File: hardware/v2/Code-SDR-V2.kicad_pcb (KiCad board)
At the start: 4 copper layers, 160 x 100 mm, 344 parts, among them J1 5V_INPUT_ONLY, J10 USB_B_Micro, J11 Cortex_SWD_10pin, J30 JK0654219NL, J50 RF_LOW_0.1_2.5GHz, J60 RF_HIGH_2.3_4.2GHz, J61 RF_HIGH_4.2_6.8GHz, J62 RF_HIGH_6.8_9.2GHz, J63 RF_HIGH_8.0_10GHz, SW1 BOOTSEL, SW2 RESET, T50 2450BL15B0200001E, T60 TC1-1-13M+, T70 2450BL15B0100001E, U1 TLV62569DBVR, U10 RP2040, U11 W25Q16JVSSIQ, U12 USBLC6-2SC6, U2 TLV62569DBVR, U20 LIF-MD6000-6JMG80I, U21 AD9215BCPZ-105, U3 TLV75525PDBVR, U30 KSZ9031RNXCA, U4 TLV76733DRVR, U40 LMX2592RHAT, U41 ADF4360-1BCPZ, U42 CDCLVC1104PWR, U50 GRF4001, U51 ADL5801ACPZ-R7, U60 GRF4001, U61 GRF2101, U62 GRF2101, U63 LTC5548IUDB, U64 QPC6144TR13, U66 GRF2101, U67 GRF2101, U70 BGS12WN6E6327, U71 GRF2013, U72 PE4312C-Z, U73 LT5560EDD, U74 AD8351ARMZ, U75 GRF2013, Y10 ABM8-272-T3_12MHz, Y30 ECS-250-20-33-TR_25MHz, Y40 SiT8209AC-23-33E-100.000000X

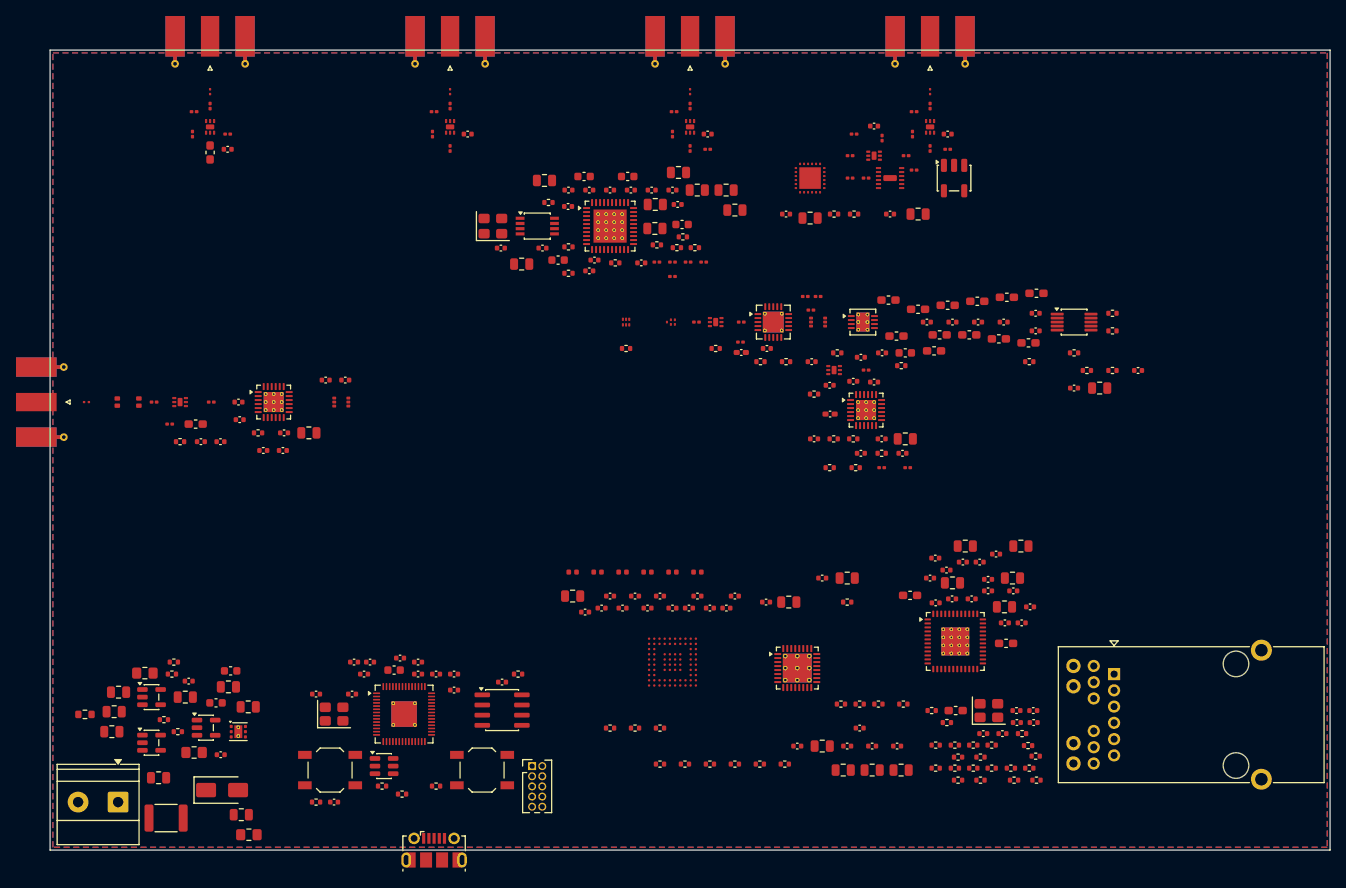
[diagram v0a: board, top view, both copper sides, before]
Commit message: hardware: finalize four-layer RF50 routing handoff
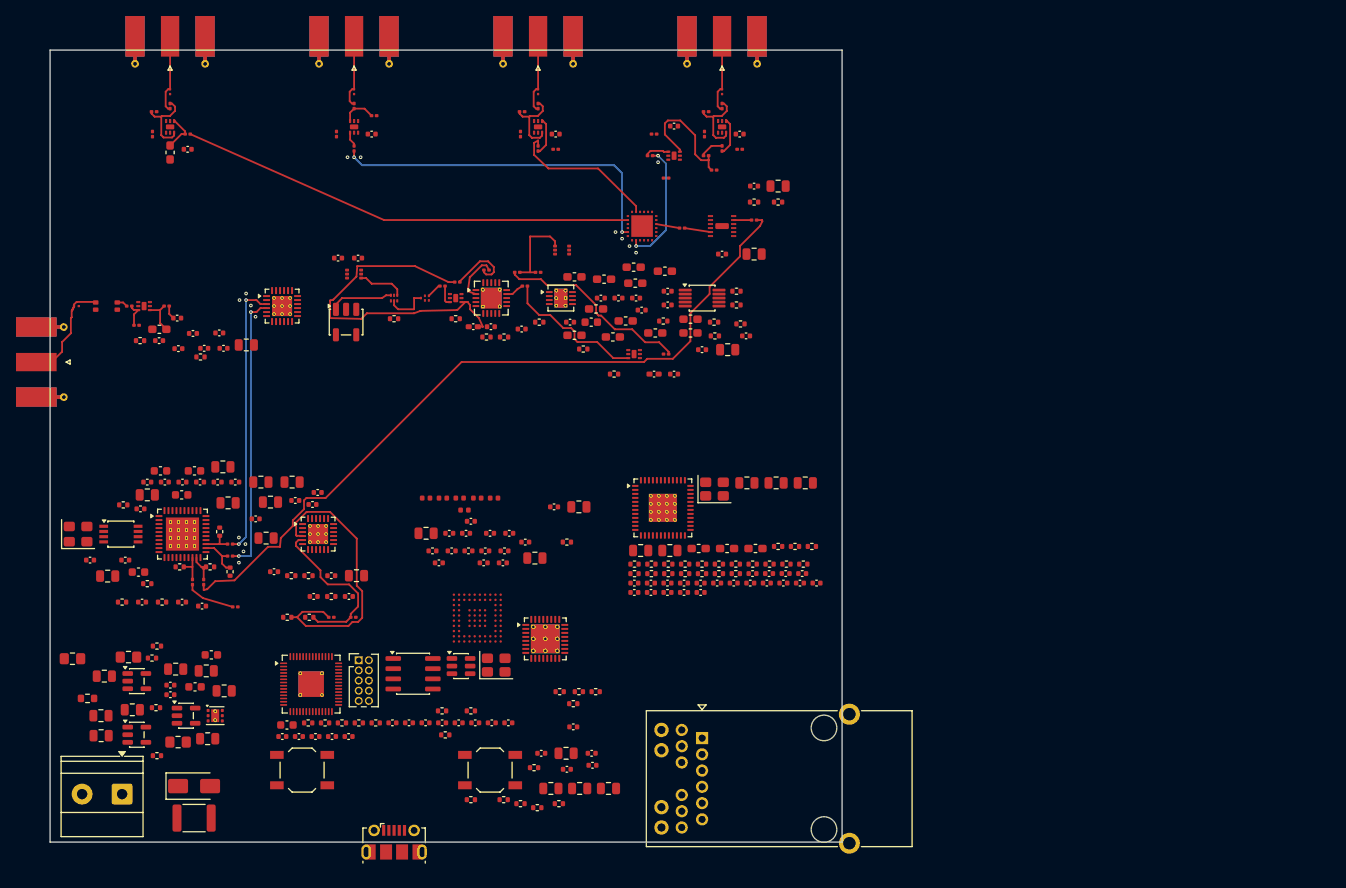
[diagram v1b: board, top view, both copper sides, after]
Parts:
- moved T60 78.1 mm to (37.0, 34.0)
- moved C71 75.4 mm to (11.5, 69.0)
- moved R56 74.8 mm to (9.00, 69.0)
- moved R53 73.9 mm to (16.2, 64.6)
- moved C202 72.1 mm to (17.8, 66.5), turned to -90 degrees
- moved C207 71.8 mm to (37.9, 70.9)
- moved C205 71.5 mm to (37.4, 68.3)
- moved C206 71.3 mm to (35.1, 70.9)
- moved R93 71.1 mm to (35.1, 68.3)
- moved C72 70.9 mm to (35.1, 65.7)
- moved R55 70.8 mm to (22.5, 65.2), turned to 90 degrees
- moved R95 70.8 mm to (32.4, 70.9)
- moved C75 70.7 mm to (33.0, 68.3)
- moved C73 70.7 mm to (38.3, 65.7)
- moved R94 70.3 mm to (29.6, 70.9)
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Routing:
- net LO_HIGH_P: track 0.00 -> 95.4 mm
- net RF_HA_LNA_OUT: track 0.00 -> 57.0 mm
- net GRF2013_RFOUT_VDD: track 0.00 -> 43.8 mm
- net RF_HB_LNA_OUT: track 0.00 -> 43.2 mm, vias 0 -> 2
- net ADF_LO2_P_RAW: track 0.00 -> 36.4 mm
- net LO_LOW_N: track 0.00 -> 34.9 mm, vias 0 -> 2
- net LO_LOW_P: track 0.00 -> 34.4 mm, vias 0 -> 2
- net IF_DSA_GAINED: track 0.00 -> 24.4 mm
- net ADF_LO2_N_RAW: track 0.00 -> 20.6 mm
- net RF_HC_LNA_OUT: track 0.00 -> 18.8 mm
- net IF_DSA_OUT: track 0.00 -> 18.2 mm
- net RF_HD_LNA_OUT: track 0.00 -> 15.7 mm, vias 0 -> 2
- net RF_HD_LNA2_IN: track 0.00 -> 15.3 mm
- net RF_LOW_IN: track 0.00 -> 11.1 mm
- net LT_INPUT_SE: track 0.00 -> 10.4 mm
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- added copper zone on In2.Cu, net GND
- removed copper zone on B.Cu, net GND
- removed copper zone on F.Cu, net GND
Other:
- board size 160 x 100 mm -> 99 x 99 mm
- board text added: "4-LAYER PLACEMENT ONLY / NO ESC"
- board text removed: "RECEIVER + CONTROL BOARD / NO ESC"

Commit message: Route and length-match Ethernet MDI pairs
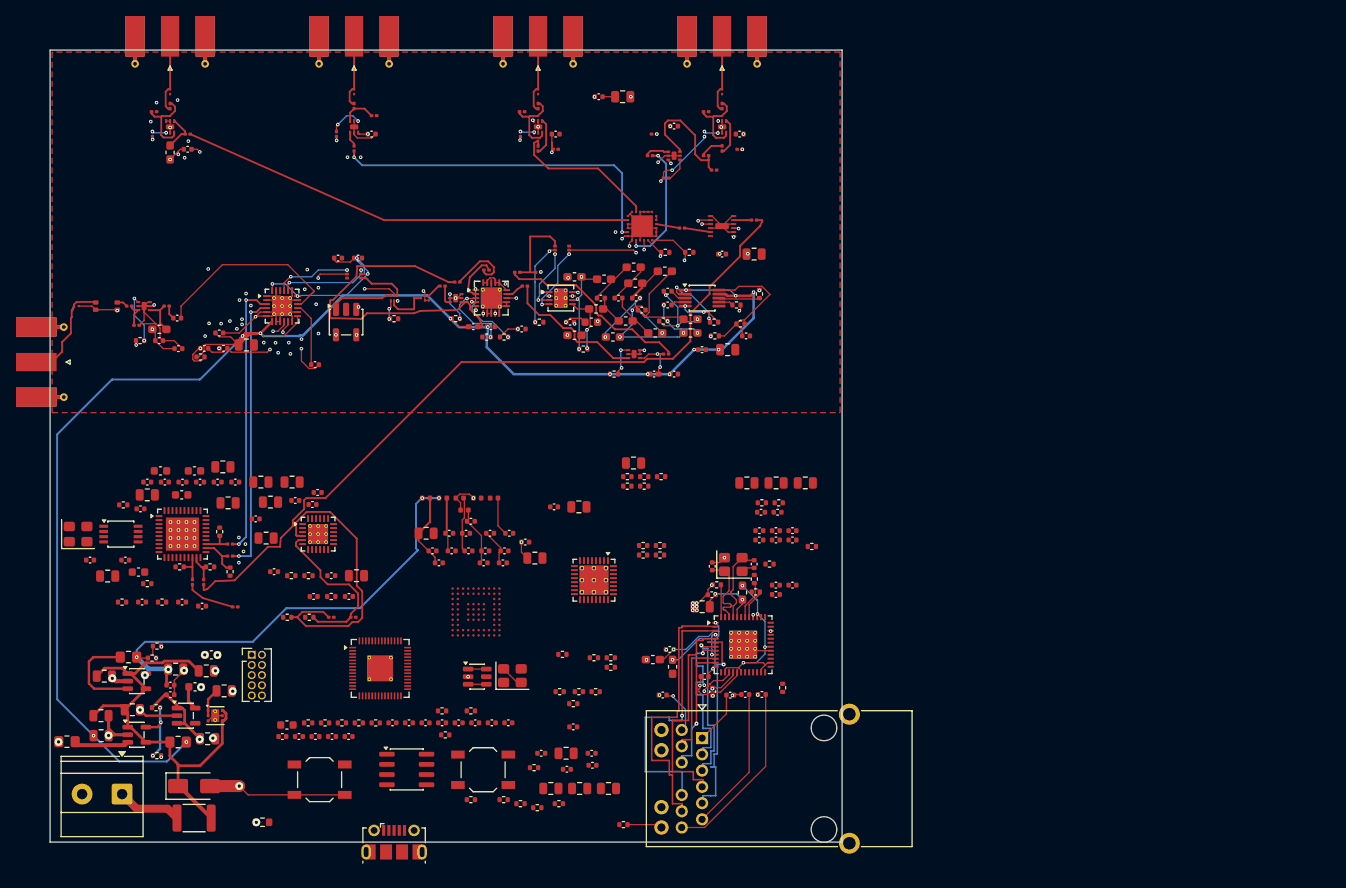
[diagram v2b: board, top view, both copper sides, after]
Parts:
- moved R42 33.6 mm to (71.7, 96.8)
- moved R5 26.8 mm to (26.6, 96.5)
- moved C260 22.4 mm to (68.6, 5.83)
- moved C261 22.4 mm to (71.6, 5.83), turned to 180 degrees
- moved C153 22.1 mm to (76.6, 80.6), turned to 180 degrees
- moved U30 19.8 mm to (86.6, 74.3)
- moved R43 19.5 mm to (70.1, 77.2)
- moved R132 19.5 mm to (68.0, 76.0)
- moved R133 19.5 mm to (70.1, 76.0)
- moved C50 18.8 mm to (82.8, 80.2), turned to -90 degrees
- moved FB32 18.1 mm to (77.8, 77.1), turned to 90 degrees
- moved C301 16.9 mm to (88.7, 60.1)
- moved C302 16.9 mm to (90.7, 60.1)
- moved C303 16.9 mm to (92.8, 60.1)
- moved C51 16.9 mm to (88.7, 61.2)
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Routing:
- net +5V_RF: track 0.00 -> 225.9 mm, vias 0 -> 18
- net GND: track 0.00 -> 202.4 mm, vias 15 -> 84
- net +1V2_CORE: track 0.00 -> 81.5 mm, vias 0 -> 8
- net +3V3_DIG: track 0.00 -> 80.8 mm, vias 0 -> 16
- net VIN_FUSED: track 0.00 -> 57.5 mm
- net IF_HIGH_P: track 0.00 -> 52.8 mm, vias 0 -> 2
- net IF_HIGH_N: track 0.00 -> 50.0 mm, vias 0 -> 2
- net MDI_A_P: track 0.00 -> 35.1 mm
- net MDI_A_N: track 0.00 -> 34.9 mm, vias 0 -> 1
- net MDI_B_P: track 0.00 -> 27.7 mm
- net MDI_B_N: track 0.00 -> 27.1 mm, vias 0 -> 1
- net PHY_LED1: track 0.00 -> 25.7 mm, vias 0 -> 1
- net ADL_RF_DRIVE: track 0.00 -> 24.7 mm
- net MAG_CT1: track 0.00 -> 22.6 mm
- net +3V3_ANA: track 0.00 -> 21.5 mm, vias 0 -> 23
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- added copper zone on In2.Cu, net +3V3_ANA
- added copper zone on In2.Cu, net +3V3_DIG
- added copper zone on F.Cu, net GND
- removed copper zone on In2.Cu, net GND

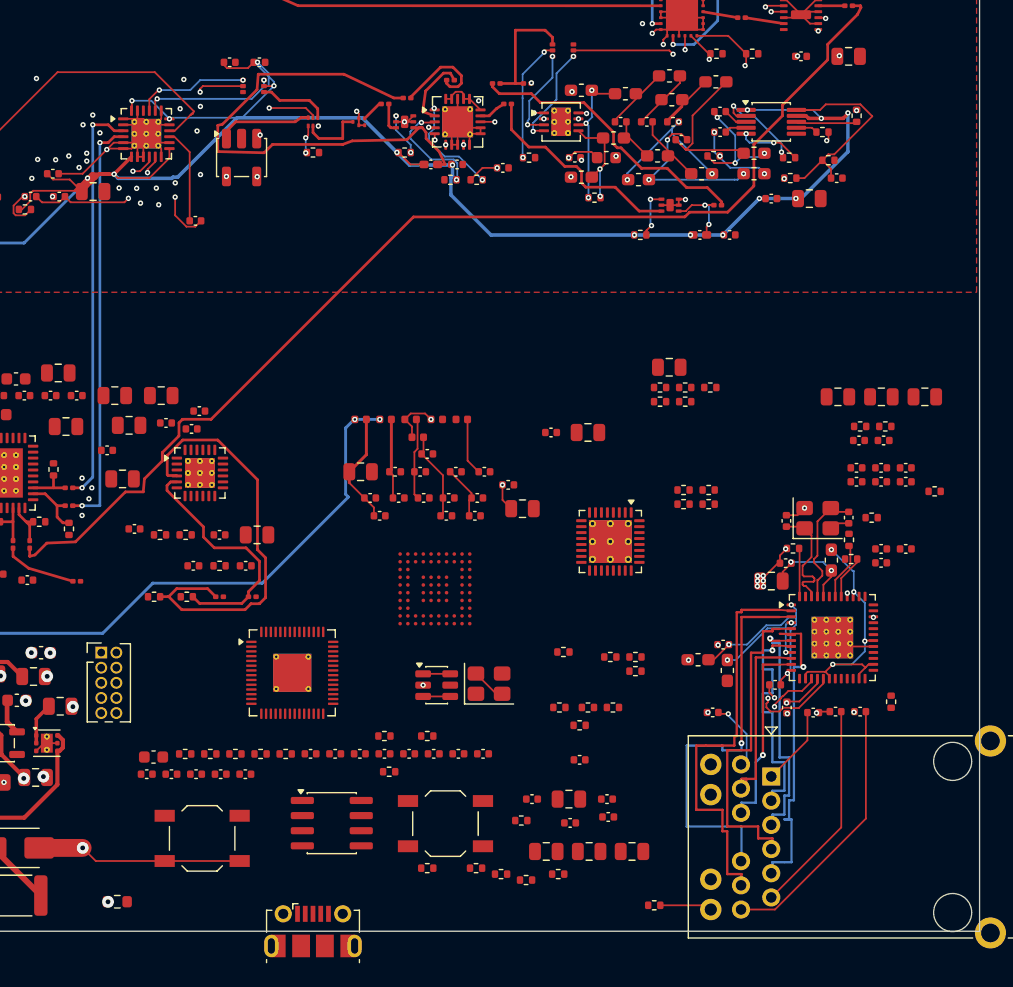
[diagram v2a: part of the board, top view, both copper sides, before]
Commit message: Route timing-critical digital and analog nets
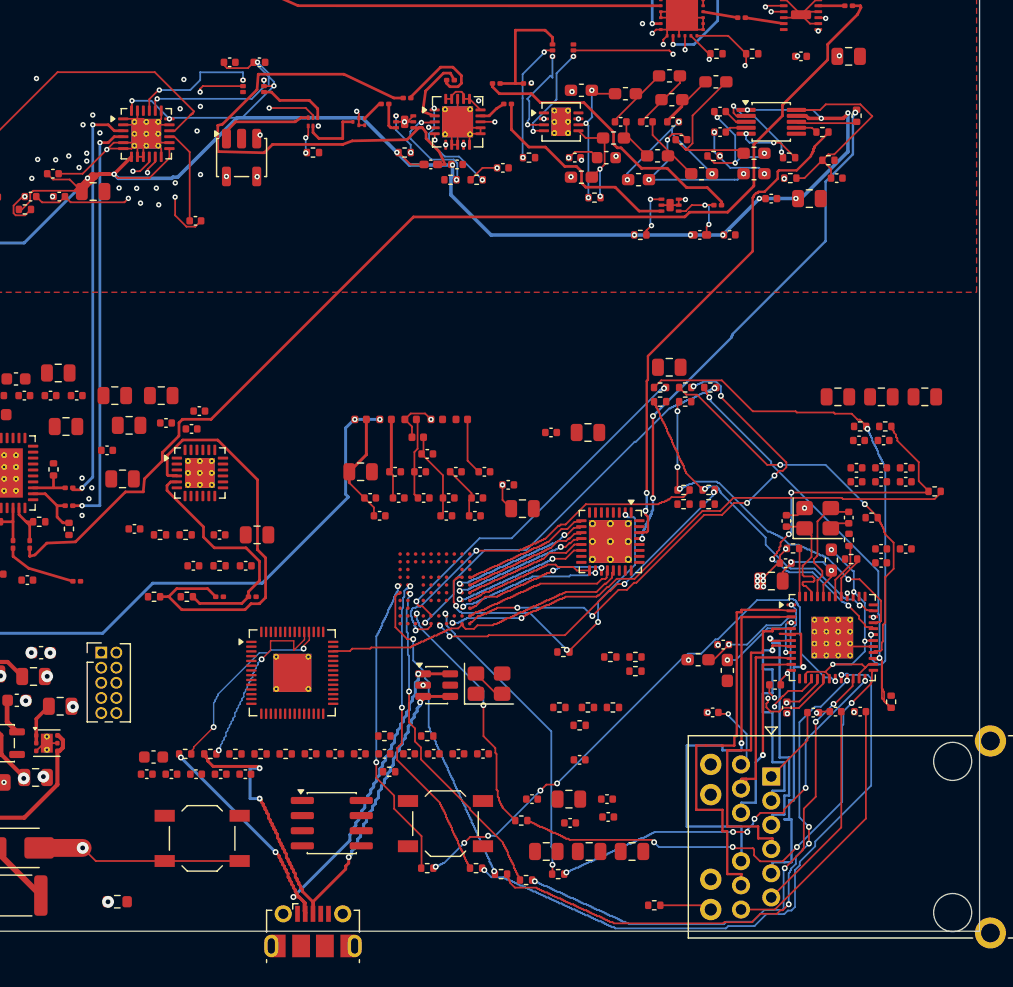
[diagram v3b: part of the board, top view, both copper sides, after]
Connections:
- U20 pad J10: (no net) -> ADC_D9
- U20 pad J4: RGMII_RXD0_FPGA -> (no net)
- U20 pad J8: ADC_D9 -> (no net)
- U20 pad J9: ADC_OR -> (no net)
- U20 pad K10: (no net) -> RGMII_RXD2_FPGA
- U20 pad K3: RGMII_RXD2_FPGA -> (no net)
- U20 pad K8: (no net) -> RGMII_RXD0_FPGA
- U20 pad K9: (no net) -> ADC_OR
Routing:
- net RGMII_TXD1: track 0.00 -> 54.0 mm, vias 0 -> 2
- net RGMII_TXD0: track 0.00 -> 48.6 mm, vias 0 -> 6
- net RGMII_TXD2: track 0.00 -> 48.3 mm, vias 0 -> 4
- net RGMII_RXD0_FPGA: track 0.00 -> 45.9 mm, vias 0 -> 2
- net RGMII_TXD3: track 0.00 -> 45.0 mm, vias 0 -> 4
- net RGMII_RXD2_FPGA: track 0.00 -> 44.6 mm, vias 0 -> 6
- net RGMII_RXD1: track 0.00 -> 43.8 mm, vias 0 -> 2
- net ADC_VIN_P: track 0.07 -> 43.7 mm, vias 1 -> 4
- net USB_DM_CONN: track 2.28 -> 45.8 mm, vias 0 -> 4
- net USB_DP_CONN: track 2.28 -> 45.4 mm, vias 0 -> 4
- net RGMII_TX_EN: track 0.00 -> 42.3 mm, vias 0 -> 4
- net ADC_VIN_N: track 0.78 -> 42.0 mm, vias 1 -> 2
- net RGMII_RXD3: track 0.00 -> 38.5 mm, vias 0 -> 2
- net RGMII_RXD0: track 0.00 -> 35.7 mm, vias 0 -> 4
- net RGMII_TXC: track 0.00 -> 34.9 mm, vias 0 -> 6
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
